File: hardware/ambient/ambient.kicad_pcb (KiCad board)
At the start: 2 copper layers, 99.1 x 50.8 mm, 54 parts, among them J1 BATT+, J2 DAQ CONN, J3 BATT-, J4 RTD CONN, J5 RTD CONN, J6 RTD CONN, J7 RTD CONN, U1 AZ1117-5.0, U2 INA125P, U3 INA125P, U4 INA125P, U5 INA125P, U6 MPXA6115A, U7 TL082, U8 MPXA6115A

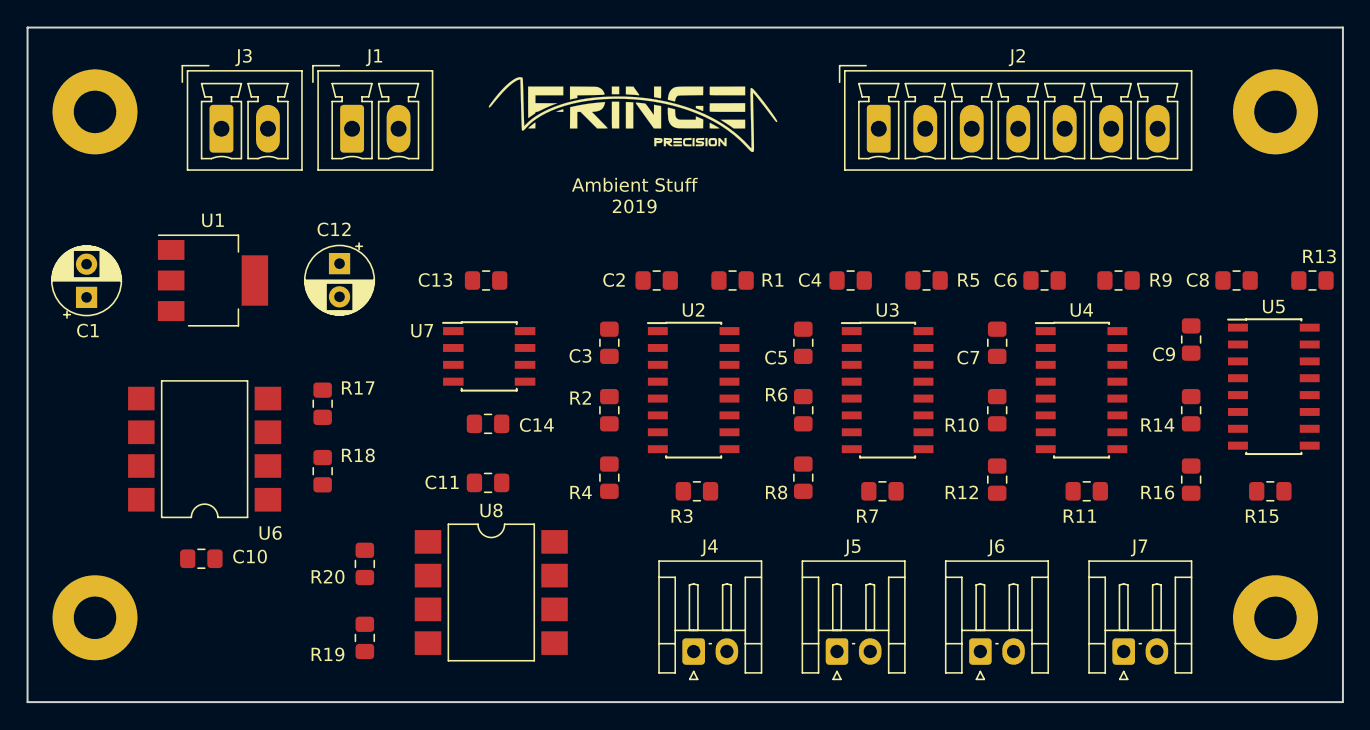
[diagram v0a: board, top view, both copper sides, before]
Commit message: Finish routing on sensor board
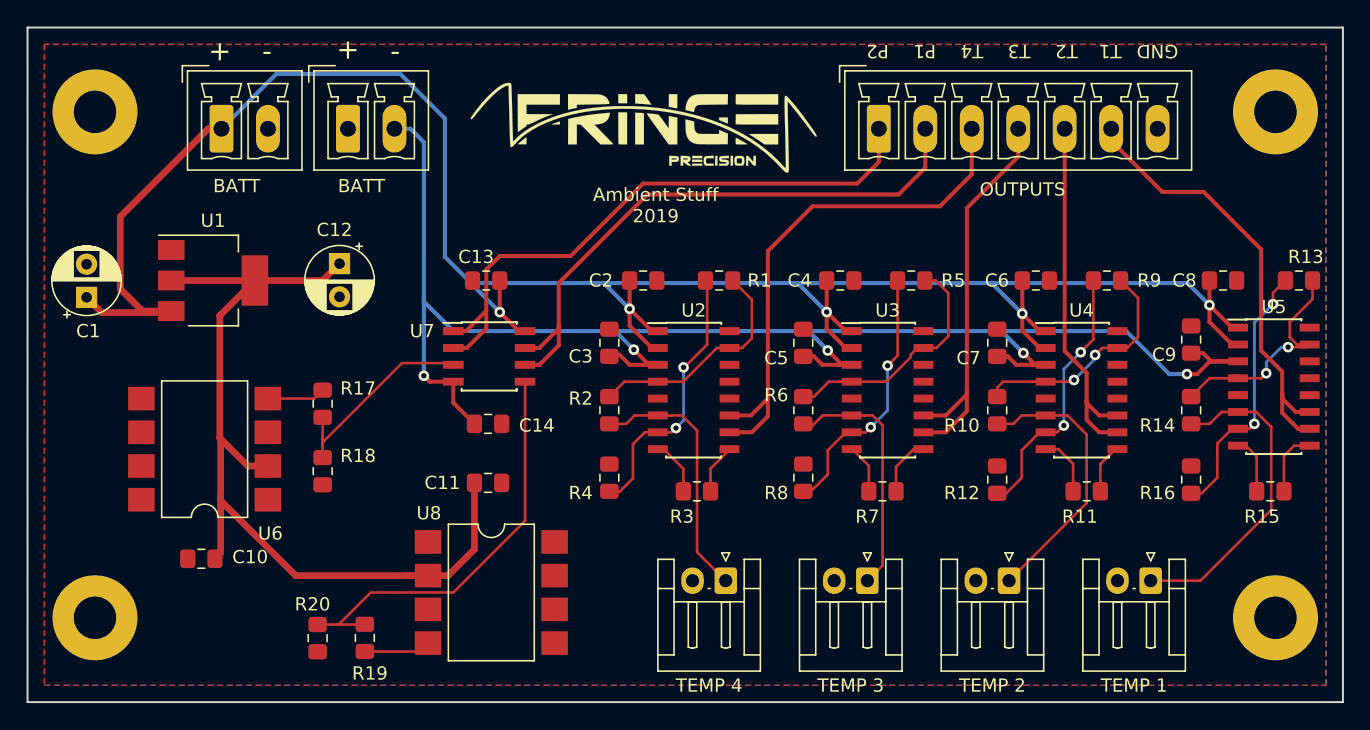
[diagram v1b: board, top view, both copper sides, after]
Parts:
- removed the G*** at (153.7, 54.6)
- removed J4, J7: RTD CONN, Connector_JST:JST_EH_S02B-EH_1x02_P2.50mm_Horizontal
- added G***: LOGO, hardware:logo_30mm, F.Cu at (154.5, 55.6)
- added TEMP 1: RTD CONN, Connector_JST:JST_EH_S02B-EH_1x02_P2.50mm_Horizontal, F.Cu at (192.5, 89.9)
- added TEMP 4: RTD CONN, Connector_JST:JST_EH_S02B-EH_1x02_P2.50mm_Horizontal, F.Cu at (160.5, 89.9)
- TEMP 2: renamed from J6
- TEMP 3: renamed from J5
- moved J1 9.83 mm to (122.6, 55.9)
- moved J3 9.53 mm to (132.1, 55.9)
- moved R20 6.62 mm to (129.8, 94.2), turned to 270 degrees
- moved TEMP 3 5.80 mm to (171.2, 89.9), turned to 180 degrees
- moved TEMP 2 5.75 mm to (181.9, 89.9), turned to 180 degrees
- moved R5 1.15 mm to (174.5, 67.3)
- moved C2 1.02 mm to (154.3, 67.3)
- moved C8 1.02 mm to (198.0, 67.3)
- moved R1 1.02 mm to (160.0, 67.3)
- moved R13 1.02 mm to (203.7, 67.3)
- moved R9 0.87 mm to (189.2, 67.3)
- moved C4 0.78 mm to (169.2, 67.3)
- moved C6 0.65 mm to (183.9, 67.3)
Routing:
- net +12V: track 0.00 -> 171.7 mm, vias 0 -> 5
- net -12V: track 0.00 -> 120.1 mm, vias 0 -> 5
- net +5V: track 0.00 -> 67.5 mm
- net /PRESSURE: track 0.00 -> 46.1 mm
- net /PRESSURE_BK: track 0.00 -> 45.4 mm
- net /RTD_AMP_1: track 0.00 -> 40.4 mm
- net /RTD_AMP_4: track 0.00 -> 34.0 mm
- net /sheet5DD1C8A8/P_BK_RAW: track 0.00 -> 31.4 mm
- net /RTD_AMP_2: track 0.00 -> 31.2 mm
- net /RTD_AMP_3: track 0.00 -> 28.1 mm
- net /sheet5DD1B5A5/RTD+: track 0.00 -> 24.4 mm
- net /sheet5DD1B4ED/RTD+: track 0.00 -> 21.0 mm
- net Net-(R1-Pad2): track 0.00 -> 20.7 mm, vias 0 -> 2
- net Net-(R13-Pad2): track 0.00 -> 20.2 mm, vias 0 -> 2
- net Net-(R12-Pad1): track 0.00 -> 20.2 mm, vias 0 -> 2
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- added copper zone on B.Cu, net GND
- added copper zone on F.Cu, net GND
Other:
- rule pad_to_mask_clearance: 0.2 -> 0.0508
- board text added: "+"
- board text added: "-"
- board text added: "BATT"
- board text added: "GND"
- board text added: "OUTPUTS"
- board text added: "P1"
- board text added: "P2"
- board text added: "T1"
- board text added: "T2"
- board text added: "T3"
- board text added: "T4"
